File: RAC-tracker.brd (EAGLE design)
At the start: 25.4 x 50.8 mm, 26 parts, among them J1 U.FL, J2 U.FL, J5 CORTEX_JTAG_DEBUG_MINIMUM_SMD, U1 NRF9160-SICA-R, U2 SIM-ST-MFF2, U3 MCP73831, U4 SKY65723-81, U5 MIC5365-1.8YC5-TR

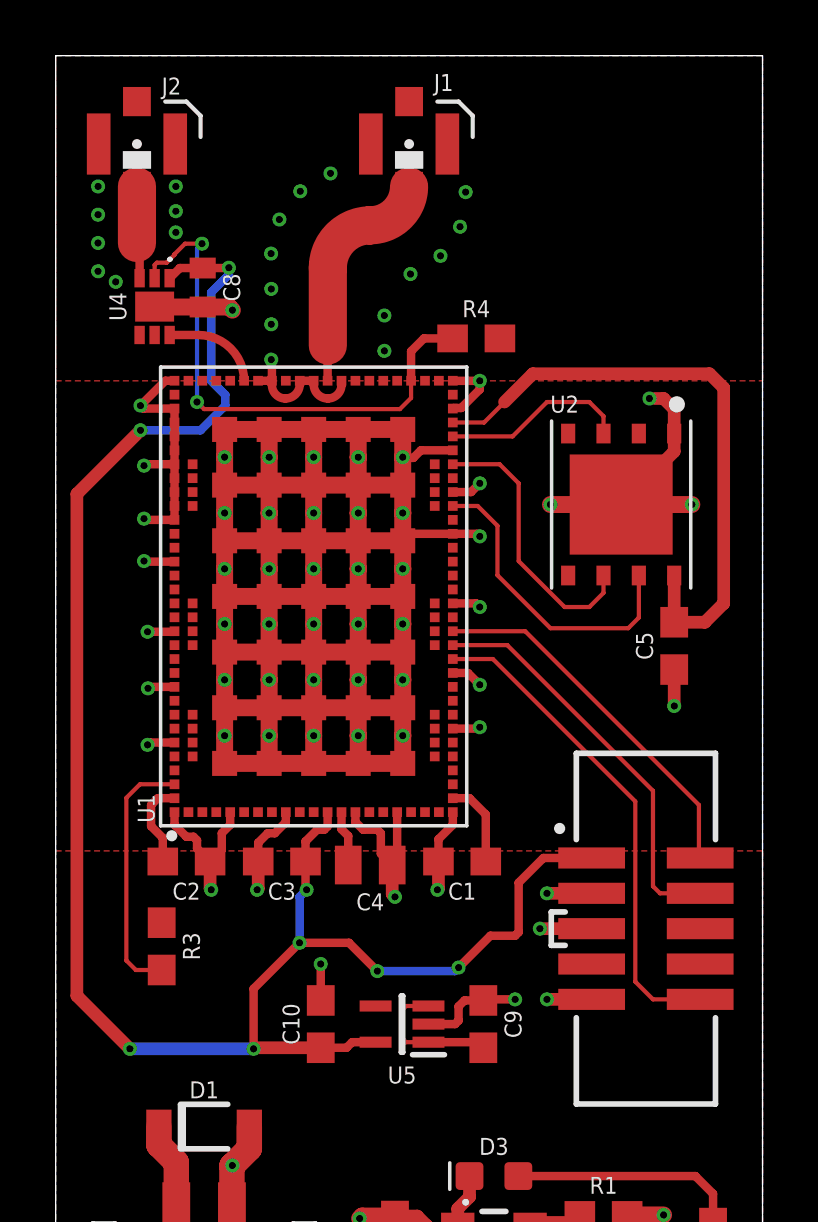
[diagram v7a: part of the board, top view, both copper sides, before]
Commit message: Stitched vias in the top ground plane. Ready for fabrication!
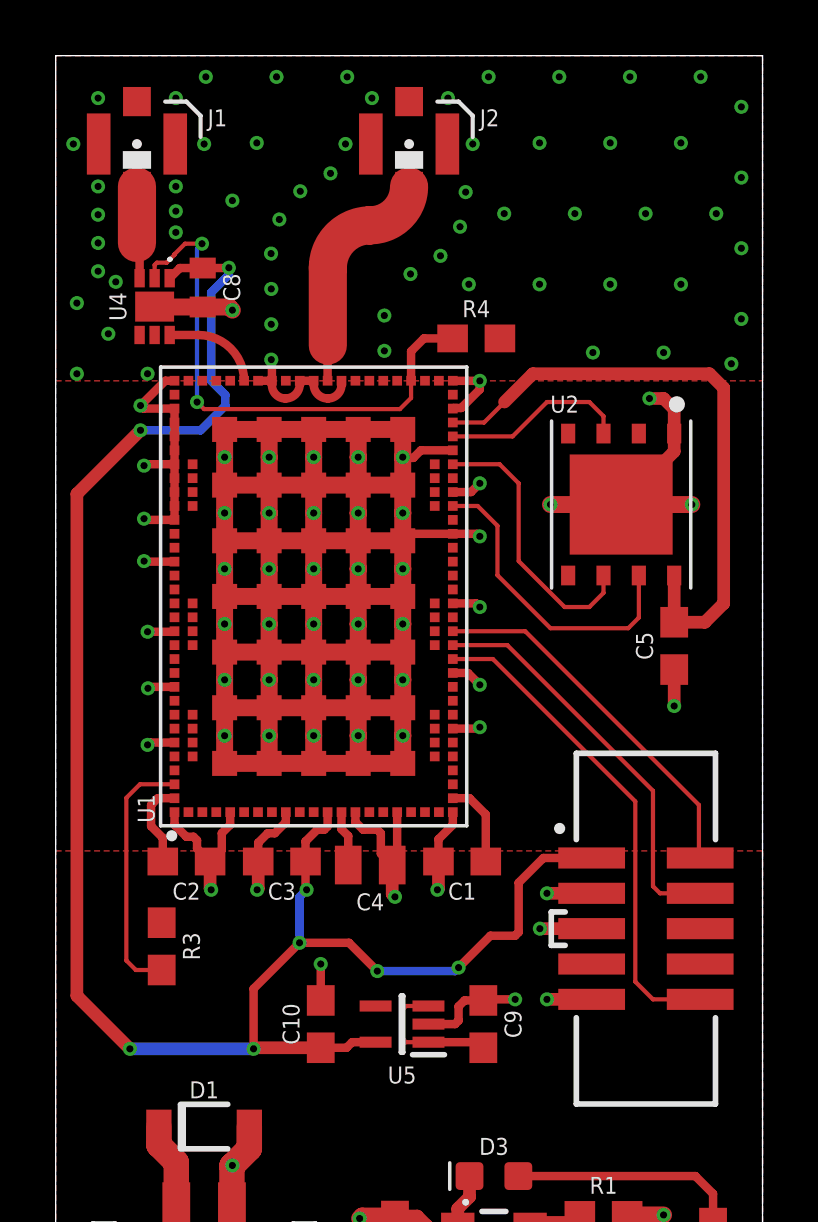
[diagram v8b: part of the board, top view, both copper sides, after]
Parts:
- moved J1 9.78 mm to (2.92, 47.6)
- moved J2 9.78 mm to (12.7, 47.6)
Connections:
- net GPS_ANT: now also J1.FEED; no longer J2.FEED
- net LTE_ANT: now also J2.FEED; no longer J1.FEED
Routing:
- net GND: vias 85 -> 124
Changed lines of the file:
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@@
 <setting verticaltext="up"/>
 </settings>
-<grid distance="50" unitdist="mil" unit="mil" style="lines" multiple="1" display="no" altdistance="5" altunitdist="mil" altunit="mil"/>
+<grid distance="5" unitdist="mil" unit="mil" style="lines" multiple="1" display="no" altdistance="1" altunitdist="mil" altunit="mil"/>
 <layers>
 <layer number="1" name="Top" color="4" fill="1" visible="yes" active="yes"/>
@@
 <layer number="44" name="Drills" color="7" fill="1" visible="no" active="yes"/>
 <layer number="45" name="Holes" color="7" fill="1" visible="no" active="yes"/>
-<layer number="46" name="Milling" color="3" fill="1" visible="no" active="yes"/>
+<layer number="46" name="Milling" color="3" fill="1" visible="yes" active="yes"/>
 <layer number="47" name="Measures" color="7" fill="1" visible="no" active="yes"/>
 <layer number="48" name="Document" color="7" fill="1" visible="no" active="yes"/>
@@
 <wire x1="0" y1="50.8" x2="0" y2="0" width="0" layer="20"/>
 <polygon width="0" layer="41">
-<vertex x="1.778" y="47.244"/>
-<vertex x="4.064" y="47.244"/>
+<vertex x="1.778" y="48.133"/>
+<vertex x="4.064" y="48.133"/>
 <vertex x="4.064" y="43.561"/>
 <vertex x="3.937" y="43.434"/>
@@
 <vertex x="3.302" y="43.307"/>
 <vertex x="3.302" y="42.926"/>
-<vertex x="2.159" y="42.926"/>
-<vertex x="2.032" y="42.926"/>
 <vertex x="1.905" y="42.926"/>
 <vertex x="1.778" y="43.053"/>
-<vertex x="1.778" y="43.18"/>
 </polygon>
 <polygon width="0" layer="41">
@@
 </class>
 </classes>
-<designrules name="oshpark-2layer *">
+<designrules name="oshpark-2layer">
 <description language="en">&lt;b&gt;OSH Park Design Rules&lt;/b&gt;
 &lt;p&gt;
@@
 <attribute name="PROD_ID" value="RES-00824" x="3.81" y="18.796" size="1.778" layer="27" rot="R90" display="off"/>
 </element>
-<element name="J1" library="SparkFun-Connectors" package="U.FL" value="U.FL" x="12.7" y="47.625" smashed="yes" rot="R270">
-<attribute name="NAME" x="13.589" y="49.53" size="0.6096" layer="25" font="vector" ratio="20"/>
+<element name="J2" library="SparkFun-Connectors" package="U.FL" value="U.FL" x="12.7" y="47.625" smashed="yes" rot="R270">
+<attribute name="NAME" x="15.24" y="48.26" size="0.6096" layer="25" font="vector" ratio="20"/>
 <attribute name="PROD_ID" value="CONN-09193" x="12.7" y="47.625" size="1.778" layer="27" rot="R270" display="off"/>
 <attribute name="SF_ID" value="WRL-09144" x="12.7" y="47.625" size="1.778" layer="27" rot="R270" display="off"/>
 </element>
-<element name="J2" library="SparkFun-Connectors" package="U.FL" value="U.FL" x="2.921" y="47.625" smashed="yes" rot="R270">
-<attribute name="NAME" x="3.81" y="49.403" size="0.6096" layer="25" font="vector" ratio="20"/>
+<element name="J1" library="SparkFun-Connectors" package="U.FL" value="U.FL" x="2.921" y="47.625" smashed="yes" rot="R270">
+<attribute name="NAME" x="5.461" y="48.26" size="0.6096" layer="25" font="vector" ratio="20"/>
 <attribute name="PROD_ID" value="CONN-09193" x="2.921" y="47.625" size="1.778" layer="27" rot="R270" display="off"/>
 <attribute name="SF_ID" value="WRL-09144" x="2.921" y="47.625" size="1.778" layer="27" rot="R270" display="off"/>
@@
 <contactref element="U1" pad="103_26"/>
 <contactref element="U1" pad="103_2"/>
+<contactref element="J2" pad="2"/>
+<contactref element="J2" pad="1"/>
 <contactref element="J1" pad="2"/>
 <contactref element="J1" pad="1"/>
-<contactref element="J2" pad="2"/>
-<contactref element="J2" pad="1"/>
 <contactref element="D1" pad="A"/>
 <contactref element="C3" pad="2"/>
@@
 <wire x1="7.747" y1="39.878" x2="7.771" y2="39.878" width="0.3048" layer="1"/>
 <wire x1="7.771" y1="39.878" x2="7.771" y2="39.119" width="0.3048" layer="1"/>
+<via x="3.302" y="39.37" extent="1-16" drill="0.254"/>
+<via x="0.762" y="39.37" extent="1-16" drill="0.254"/>
+<via x="0.762025" y="41.91" extent="1-16" drill="0.254"/>
+<via x="19.304" y="40.132" extent="1-16" drill="0.254"/>
+<via x="21.844" y="40.132" extent="1-16" drill="0.254"/>
+<via x="24.278790625" y="39.729209375" extent="1-16" drill="0.254"/>
+<via x="24.63801875" y="41.34036875" extent="1-16" drill="0.254"/>
+<via x="24.63804375" y="43.88036875" extent="1-16" drill="0.254"/>
+<via x="24.638071875" y="46.42036875" extent="1-16" drill="0.254"/>
+<via x="24.638096875" y="48.96036875" extent="1-16" drill="0.254"/>
+<via x="23.17563125" y="50.038" extent="1-16" drill="0.254"/>
+<via x="20.63563125" y="50.038" extent="1-16" drill="0.254"/>
+<via x="18.09563125" y="50.038" extent="1-16" drill="0.254"/>
+<via x="15.55563125" y="50.038" extent="1-16" drill="0.254"/>
+<via x="11.36463125" y="49.276" extent="1-16" drill="0.254"/>
+<via x="10.47563125" y="50.038" extent="1-16" drill="0.254"/>
+<via x="7.93563125" y="50.038" extent="1-16" drill="0.254"/>
+<via x="5.39563125" y="50.038" extent="1-16" drill="0.254"/>
+<via x="1.524" y="49.276" extent="1-16" drill="0.254"/>
+<via x="4.318" y="49.276" extent="1-16" drill="0.254"/>
+<via x="5.334" y="47.625" extent="1-16" drill="0.254"/>
+<via x="0.635" y="47.625" extent="1-16" drill="0.254"/>
+<via x="14.097" y="49.276" extent="1-16" drill="0.254"/>
+<via x="14.986" y="47.625" extent="1-16" drill="0.254"/>
+<via x="10.414" y="47.625" extent="1-16" drill="0.254"/>
+<via x="1.8923" y="40.806" extent="1-16" drill="0.254"/>
+<via x="7.2263" y="47.664" extent="1-16" drill="0.254"/>
+<via x="14.8463" y="42.584" extent="1-16" drill="0.254"/>
+<via x="16.1163" y="45.124" extent="1-16" drill="0.254"/>
+<via x="17.3863" y="42.584" extent="1-16" drill="0.254"/>
+<via x="18.6563" y="45.124" extent="1-16" drill="0.254"/>
+<via x="17.3863" y="47.664" extent="1-16" drill="0.254"/>
+<via x="19.9263" y="42.584" extent="1-16" drill="0.254"/>
+<via x="21.1963" y="45.124" extent="1-16" drill="0.254"/>
+<via x="19.9263" y="47.664" extent="1-16" drill="0.254"/>
+<via x="22.4663" y="42.584" extent="1-16" drill="0.254"/>
+<via x="23.7363" y="45.124" extent="1-16" drill="0.254"/>
+<via x="22.4663" y="47.664" extent="1-16" drill="0.254"/>
+<via x="6.35" y="45.593" extent="1-16" drill="0.254"/>
 </signal>
 <signal name="SIM_VIN">
@@
 <signal name="LTE_ANT">
 <contactref element="U1" pad="61"/>
-<contactref element="J1" pad="FEED"/>
+<contactref element="J2" pad="FEED"/>
 <wire x1="12.7" y1="46.1" x2="11.304" y2="44.704" width="1.3716" layer="1" curve="-90"/>
 <wire x1="11.304" y1="44.704" x2="11.303" y2="44.704" width="1.3716" layer="1"/>
@@
 </signal>
 <signal name="GPS_ANT">
-<contactref element="J2" pad="FEED"/>
+<contactref element="J1" pad="FEED"/>
 <contactref element="U4" pad="3"/>
 <wire x1="3.016" y1="42.803" x2="3.016" y2="43.974" width="0.3048" layer="1"/>
@@
 <wire x1="10.653" y1="15.352" x2="10.453" y2="15.152" width="0.3048" layer="1"/>
 <contactref element="J5" pad="1"/>
-<wire x1="9.525" y1="15.152" x2="9.486" y2="15.113" width="0.4572" layer="1"/>
 <wire x1="9.771" y1="23.619" x2="9.771" y2="23.106" width="0.3048" layer="1"/>
 <wire x1="9.652" y1="22.987" x2="9.771" y2="23.106" width="0.3048" layer="1"/>
